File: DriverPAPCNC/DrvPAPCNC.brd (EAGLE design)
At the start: 160 x 100 mm, 33 parts, among them IC1 ATMEGA168-20P, K1 G5LE, Q1 16MHz

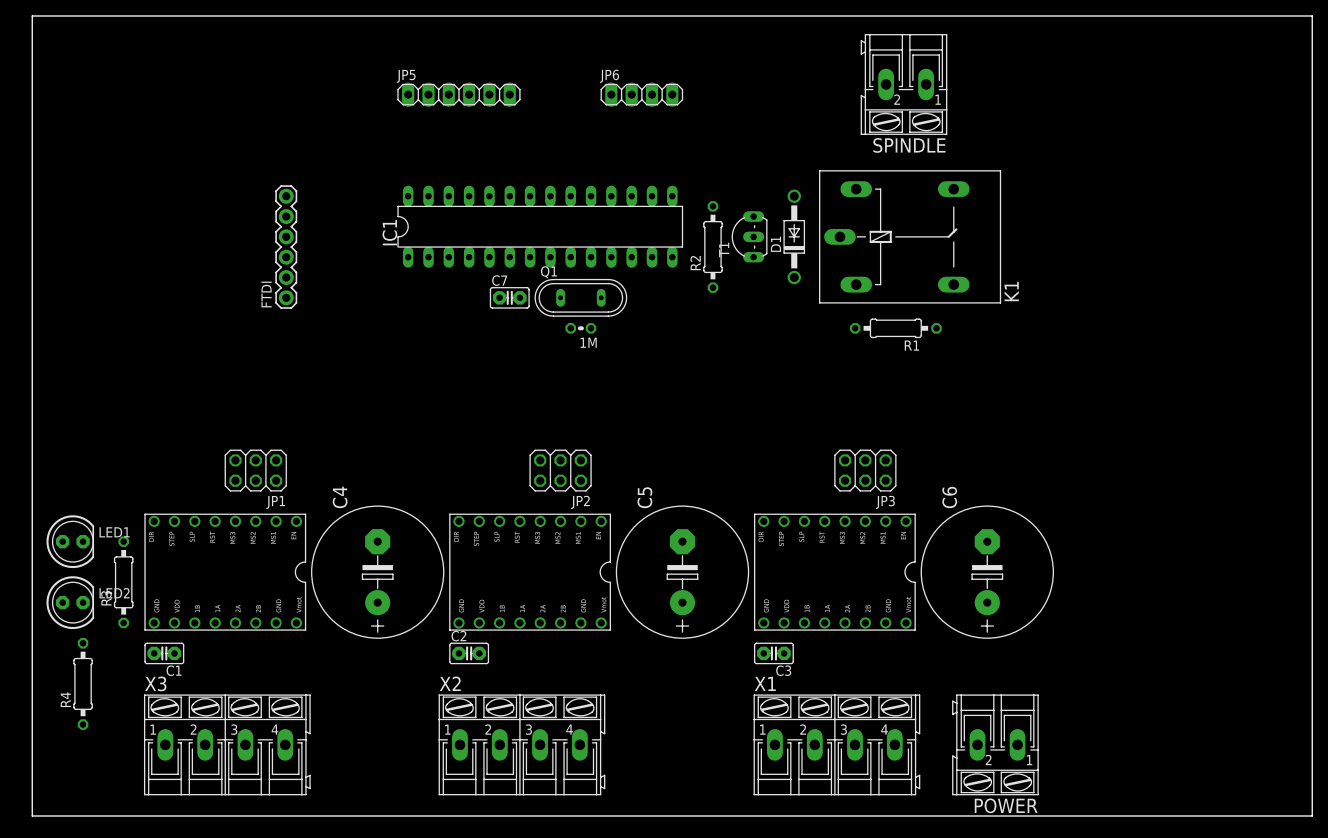
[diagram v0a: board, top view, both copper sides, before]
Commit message: Finish Route PCB one layer
Finish Route PCB one layer.
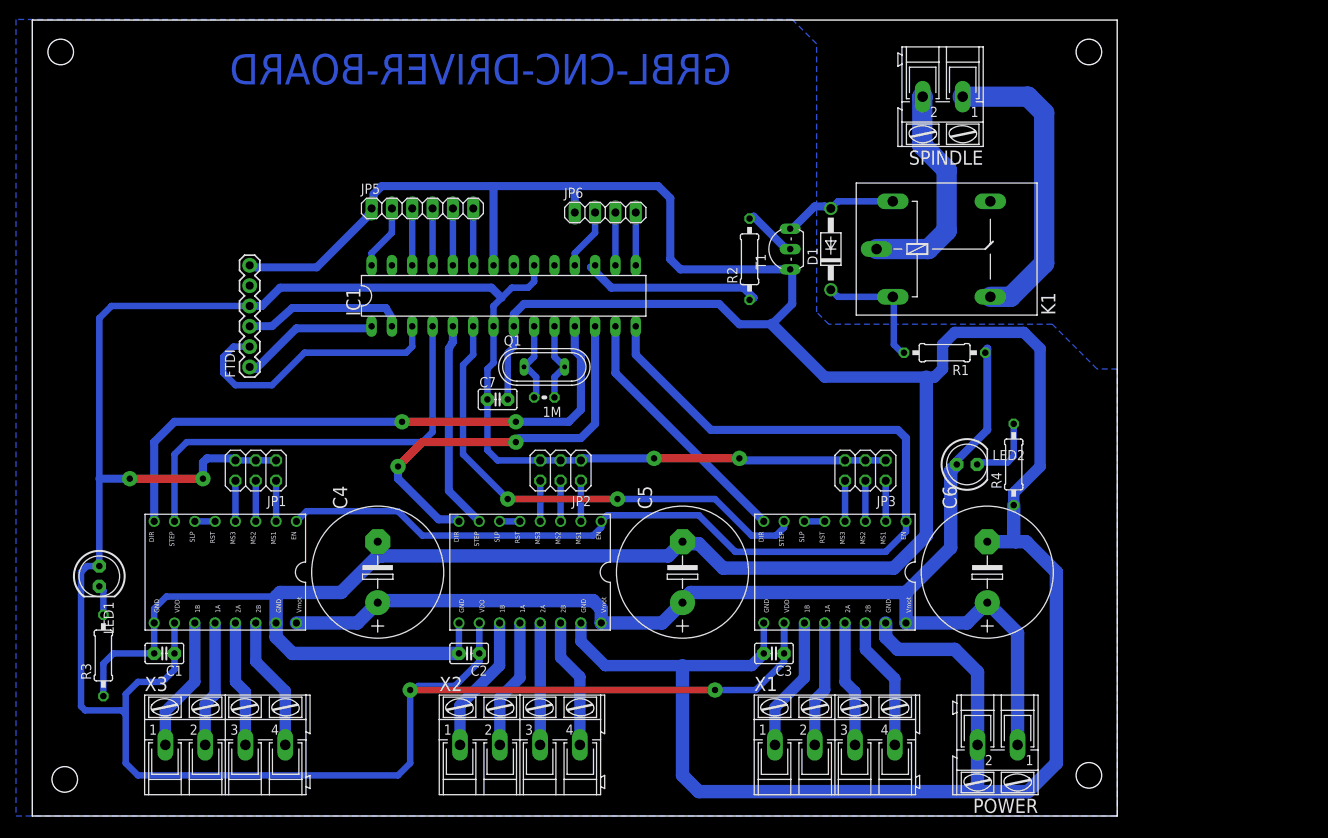
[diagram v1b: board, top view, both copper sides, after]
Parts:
- moved R4 119.5 mm to (122.7, 43.9)
- moved LED2 113.1 mm to (116.8, 43.9)
- moved JP6 15.4 mm to (71.6, 75.4)
- moved JP5 14.9 mm to (48.8, 75.9)
- moved C7 12.8 mm to (58.2, 52.1)
- moved 1M 9.77 mm to (64.0, 52.3)
- moved IC1 9.77 mm to (58.9, 65.0)
- moved Q1 9.77 mm to (64.0, 56.1)
- moved FTDI 9.77 mm to (27.2, 56.1)
- moved R3 9.49 mm to (8.89, 20.1)
- moved R1 6.82 mm to (114.0, 57.9)
- moved LED1 5.44 mm to (8.38, 30.0), turned to 270 degrees
- moved D1 4.82 mm to (99.8, 70.9)
- moved K1 4.82 mm to (115.1, 70.9)
- moved R2 4.82 mm to (89.7, 69.6)
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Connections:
- removed net N$15: JP3.1, JP3.3, JP3.5
- net VDD: now also JP3.1, JP3.3, JP3.5
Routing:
- net GND: track 0.00 -> 550.5 mm
- net VDD: track 0.00 -> 350.4 mm, vias 0 -> 6
- net +36V: track 0.00 -> 151.3 mm
- net ENABLE: track 0.00 -> 135.8 mm
- net XDIR: track 0.00 -> 75.7 mm, vias 0 -> 2
- net ZPULSE: track 0.00 -> 62.1 mm, vias 0 -> 2
- net XPULSE: track 0.00 -> 55.0 mm
- net YDIR: track 0.00 -> 50.4 mm, vias 0 -> 2
- net N$14: track 0.00 -> 38.3 mm
- net RXI: track 0.00 -> 34.7 mm
- net ZDIR: track 0.00 -> 32.1 mm
- net N$13: track 0.00 -> 27.8 mm
- net YPULSE: track 0.00 -> 26.1 mm
- net PWMSPINDLE: track 0.00 -> 23.0 mm
- net TXO: track 0.00 -> 20.4 mm
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- added copper zone on layer 16, net GND
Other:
- board size 160 x 100 mm -> 135.6 x 99.5 mm
- board text added: "GRBL-CNC-DRIVER-BOARD"
